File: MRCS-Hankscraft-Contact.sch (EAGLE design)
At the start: 6 parts, among them K2 TN2-4.5V

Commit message: First release sent out to fab
I'll send these to Allison for testing
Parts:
- removed OSHW1: DOC-OSHW-LOGO-M, SPCoast:DOC-OSHW-LOGO-M
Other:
- note removed: "A Template for Eagle Projects"
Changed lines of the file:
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@@
 <parts>
 <part name="FRAME1" library="SPCoast" deviceset="DOC-FRAME-LETTER" device=""/>
-<part name="OSHW1" library="SPCoast" deviceset="DOC-OSHW-LOGO-" device="M"/>
 <part name="K2" library="relay" deviceset="TN2?-*" device="" technology="4.5V"/>
 <part name="PWR" library="SPCoast" deviceset="CONNECTOR-M02" device="1X02-LOCK"/>
@@
 <sheet>
 <plain>
-<text x="152.4" y="20.32" size="2.1844" layer="97">A Template for Eagle Projects</text>
 <text x="240.03" y="12.7" size="2.1844" layer="97">1.0</text>
 <text x="241.3" y="6.35" size="2.1844" layer="97">A</text>
@@
 <instance part="FRAME1" gate="FRAME" x="0" y="0"/>
 <instance part="FRAME1" gate="FRAME_CONTENT" x="147.32" y="0"/>
-<instance part="OSHW1" gate="DOC-OSHW-LOGO" x="233.68" y="38.1"/>
 <instance part="K2" gate="-" x="81.28" y="142.24"/>
 <instance part="K2" gate="1" x="66.04" y="96.52" rot="R270"/>

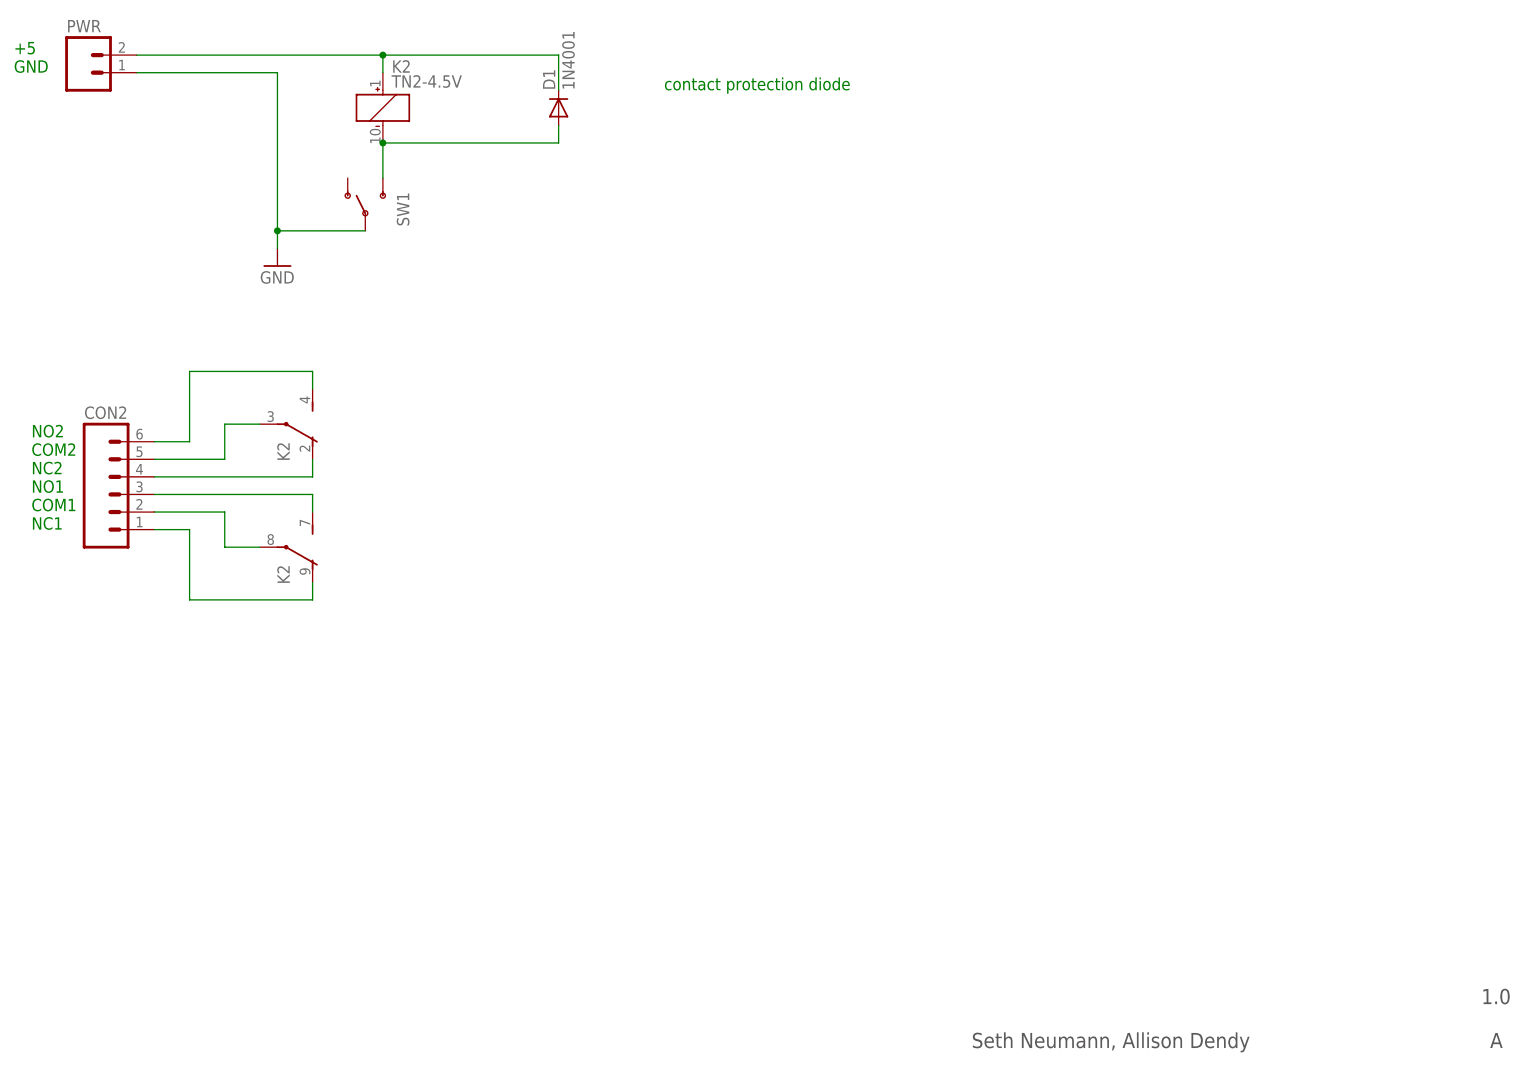
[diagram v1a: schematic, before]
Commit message: Version 2
changed size to give the uSwitch pads more room, removed footprint for toggle switch, just using test point pads for connections.
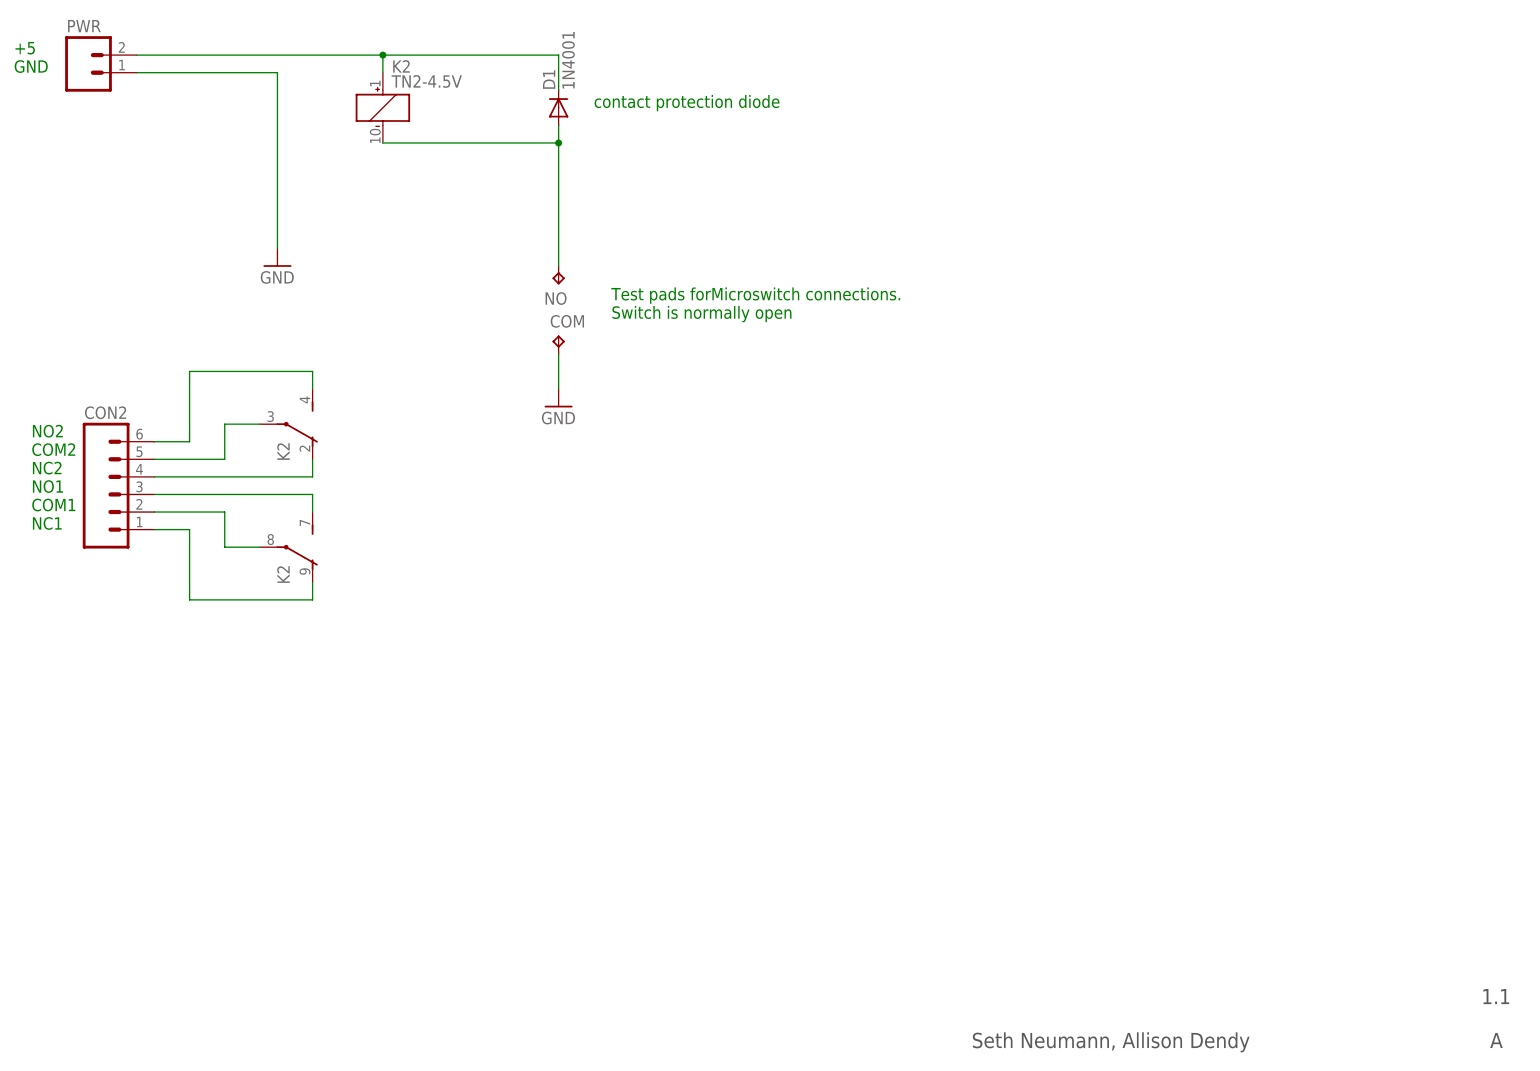
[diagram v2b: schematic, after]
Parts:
- removed SW1: (no value), SPCoast:SWITCH-SPSTPTH
- added COM, NO: TPPAD1-17, testpad:TPPAD1-17
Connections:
- net GND: now also COM.TP; no longer SW1.P
- net N$9: now also NO.TP; no longer SW1.S
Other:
- note added: "1.1"
- note added: "Test pads forMicroswitch connections. Switch is normally open"
- note removed: "1.0"
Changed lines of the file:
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@@
 <part name="PWR" library="SPCoast" deviceset="CONNECTOR-M02" device="1X02-LOCK"/>
 <part name="CON2" library="SPCoast" deviceset="CONNECTOR-M06" device="LOCK"/>
-<part name="SW1" library="SPCoast" deviceset="SWITCH-SPST" device="PTH"/>
 <part name="D1" library="SPCoast" deviceset="DIODE" device="PTH" value="1N4001"/>
 <part name="GND1" library="SPCoast" deviceset="GND" device=""/>
+<part name="GND2" library="SPCoast" deviceset="GND" device=""/>
+<part name="COM" library="testpad" deviceset="TP" device="PAD1-17"/>
+<part name="NO" library="testpad" deviceset="TP" device="PAD1-17"/>
 </parts>
 <sheets>
 <sheet>
 <plain>
-<text x="240.03" y="12.7" size="2.1844" layer="97">1.0</text>
+<text x="240.03" y="12.7" size="2.1844" layer="97">1.1</text>
 <text x="241.3" y="6.35" size="2.1844" layer="97">A</text>
 <text x="166.37" y="6.35" size="2.1844" layer="97">Seth Neumann, Allison Dendy</text>
 <text x="27.94" y="147.32" size="1.778" layer="91">+5
 GND</text>
-<text x="121.92" y="144.78" size="1.778" layer="91">contact protection diode</text>
+<text x="111.76" y="142.24" size="1.778" layer="91">contact protection diode</text>
 <text x="30.48" y="81.28" size="1.778" layer="91">NO2
 COM2
@@
 COM1
 NC1</text>
+<text x="114.3" y="111.76" size="1.778" layer="91">Test pads forMicroswitch connections.
+Switch is normally open</text>
 </plain>
 <instances>
@@
 <instance part="PWR" gate="J" x="40.64" y="147.32"/>
 <instance part="CON2" gate="J" x="43.18" y="86.36"/>
-<instance part="SW1" gate="1" x="78.74" y="127" rot="R90"/>
 <instance part="D1" gate="D1" x="106.68" y="142.24" rot="R90"/>
 <instance part="GND1" gate="1" x="66.04" y="119.38"/>
+<instance part="GND2" gate="1" x="106.68" y="99.06"/>
+<instance part="COM" gate="G$1" x="106.68" y="109.22"/>
+<instance part="NO" gate="G$1" x="106.68" y="116.84" rot="R180"/>
 </instances>
 <busses>
@@
 <segment>
 <pinref part="K2" gate="-" pin="-"/>
-<pinref part="SW1" gate="1" pin="S"/>
-<wire x1="81.28" y1="132.08" x2="81.28" y2="137.16" width="0.1524" layer="91"/>
 <wire x1="81.28" y1="137.16" x2="106.68" y2="137.16" width="0.3048" layer="91"/>
 <pinref part="D1" gate="D1" pin="A"/>
 <wire x1="106.68" y1="139.7" x2="106.68" y2="137.16" width="0.3048" layer="91"/>
-<junction x="81.28" y="137.16"/>
+<wire x1="106.68" y1="137.16" x2="106.68" y2="119.38" width="0.3048" layer="91"/>
+<pinref part="NO" gate="G$1" pin="TP"/>
+<junction x="106.68" y="137.16"/>
 </segment>
 </net>
@@
 <pinref part="PWR" gate="J" pin="A"/>
 <wire x1="45.72" y1="147.32" x2="66.04" y2="147.32" width="0.3048" layer="91"/>
-<wire x1="66.04" y1="147.32" x2="66.04" y2="124.46" width="0.3048" layer="91"/>
-<wire x1="66.04" y1="124.46" x2="78.74" y2="124.46" width="0.3048" layer="91"/>
-<pinref part="SW1" gate="1" pin="P"/>
+<wire x1="66.04" y1="147.32" x2="66.04" y2="121.92" width="0.3048" layer="91"/>
 <pinref part="GND1" gate="1" pin="GND"/>
-<wire x1="66.04" y1="124.46" x2="66.04" y2="121.92" width="0.3048" layer="91"/>
-<junction x="66.04" y="124.46"/>
+</segment>
+<segment>
+<pinref part="GND2" gate="1" pin="GND"/>
+<wire x1="106.68" y1="106.68" x2="106.68" y2="101.6" width="0.3048" layer="91"/>
+<pinref part="COM" gate="G$1" pin="TP"/>
 </segment>
 </net>

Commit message: adding back to Github - disappeared
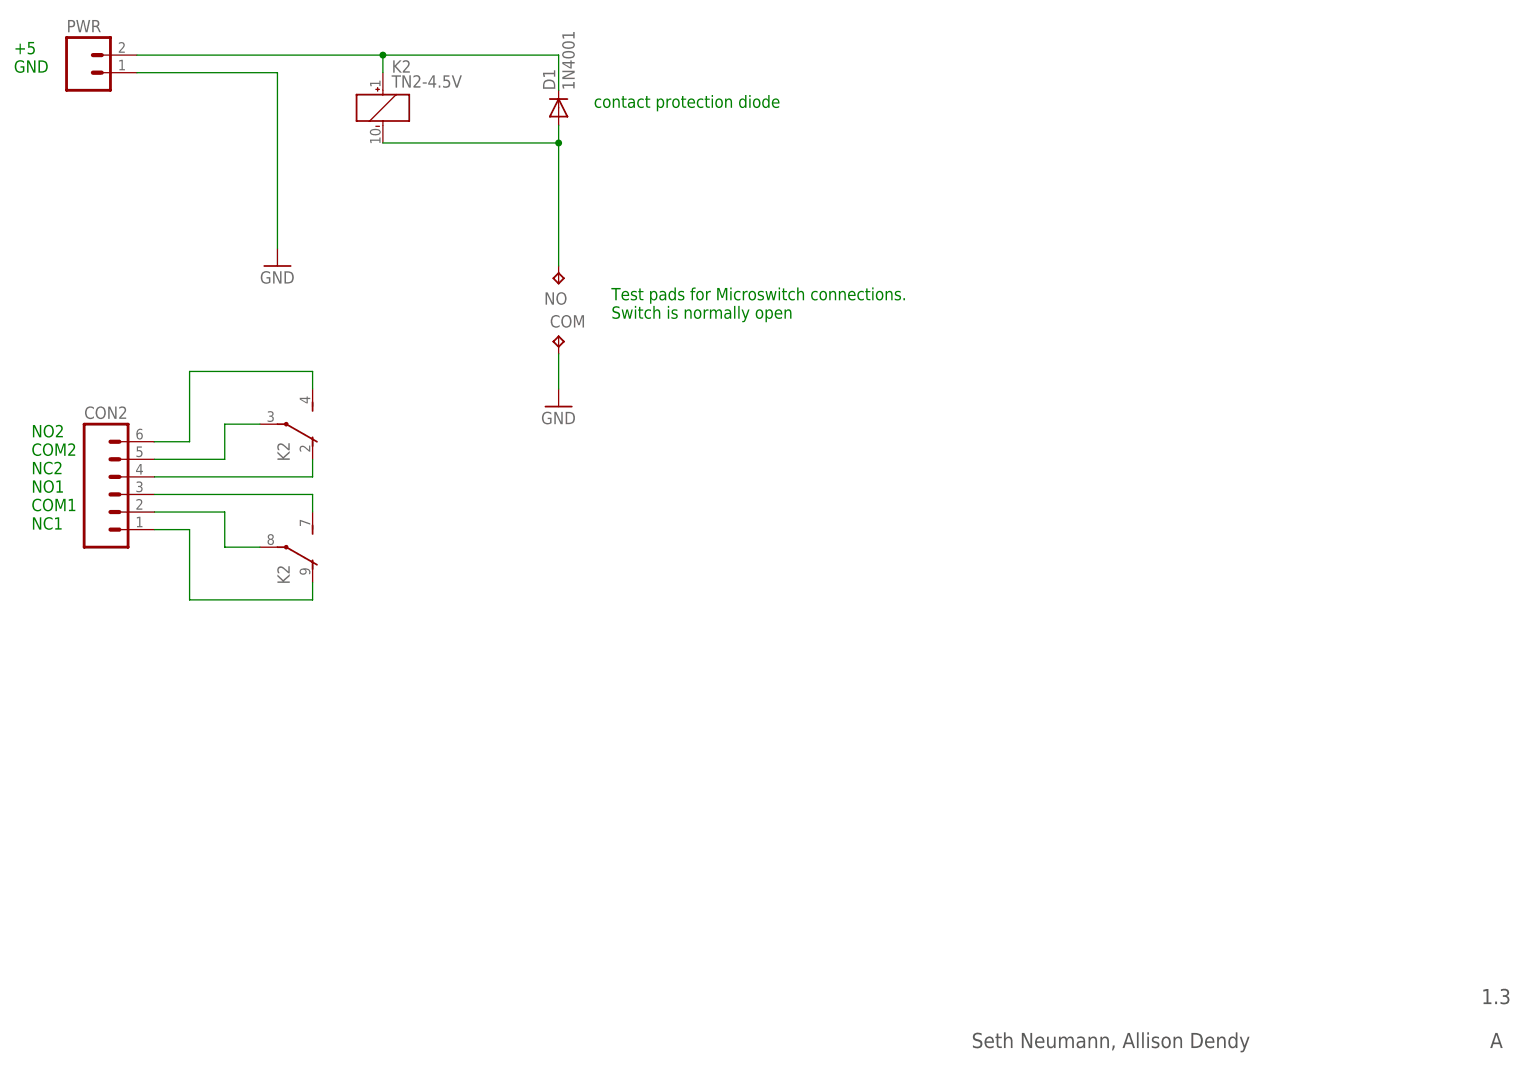
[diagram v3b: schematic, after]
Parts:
- COM, NO: value TPPAD1-17 -> TPPAD1-13; device testpad:TPPAD1-17 -> testpad:TPPAD1-13
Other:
- note added: "1.3"
- note added: "Test pads for Microswitch connections. Switch is normally open"
- note removed: "1.1"
- note removed: "Test pads forMicroswitch connections. Switch is normally open"
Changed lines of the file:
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@@
 <part name="GND1" library="SPCoast" deviceset="GND" device=""/>
 <part name="GND2" library="SPCoast" deviceset="GND" device=""/>
-<part name="COM" library="testpad" deviceset="TP" device="PAD1-17"/>
-<part name="NO" library="testpad" deviceset="TP" device="PAD1-17"/>
+<part name="COM" library="testpad" deviceset="TP" device="PAD1-13" value="TPPAD1-13"/>
+<part name="NO" library="testpad" deviceset="TP" device="PAD1-13" value="TPPAD1-13"/>
 </parts>
 <sheets>
 <sheet>
 <plain>
-<text x="240.03" y="12.7" size="2.1844" layer="97">1.1</text>
+<text x="240.03" y="12.7" size="2.1844" layer="97">1.3</text>
 <text x="241.3" y="6.35" size="2.1844" layer="97">A</text>
 <text x="166.37" y="6.35" size="2.1844" layer="97">Seth Neumann, Allison Dendy</text>
@@
 COM1
 NC1</text>
-<text x="114.3" y="111.76" size="1.778" layer="91">Test pads forMicroswitch connections.
+<text x="114.3" y="111.76" size="1.778" layer="91">Test pads for Microswitch connections.
 Switch is normally open</text>
 </plain>
